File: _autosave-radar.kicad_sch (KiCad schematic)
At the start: 3 parts, among them J1 USB_C_Receptacle, J2 Conn_01x02_Pin, U1 BQ25895RTW

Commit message: expanding size of schematic
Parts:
- removed J2: Conn_01x02_Pin, symbol Connector:Conn_01x02_Pin
- added BT1: Battery_Cell, symbol Device:Battery_Cell
- added C1: 0.047muF, symbol Device:C
- added L1: 2.2muH, symbol Device:L
- added R1: 30K, symbol Device:R_US
- added R1: 5K, symbol Device:R_US
- added R3: 20muF, symbol Device:R_US
- added TH1: 103AT, symbol Device:Thermistor_NTC_US
- added U2: TPS61022, Package_DFN_QFN:Texas_RWU0007A_VQFN-7_2x2mm_P0.5mm, symbol Converter_DCDC:TPS61022
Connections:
- net GND: now reaches J1.A1 (GND), J1.A12 (GND), J1.B1 (GND), J1.B12 (GND)
- net GND: now also U1.17 (PGND), U1.18 (PGND), U1.25 (PGND), U1.8 (OTG), R1.1, TH1.1, U2.1 (GND)
- net at J1.A4 (VBUS), J1.A9 (VBUS), J1.B4 (VBUS)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: now also U1.1 (VBUS)
- net at U1.11 (TS): now also R1.1, R1.2
- net at U1.13 (BAT), U1.14 (BAT): now also BT1.2 (-)
- net at U1.15 (SYS), U1.16 (SYS): now also C1.1, R3.2
- net at U1.19 (SW), U1.20 (SW): now also L1.2
- net at U1.2 (D+): now also U1.3 (D-)
- net at U1.21 (BTST): now also C1.2
- net at U1.22 (REGN): now also R1.2, TH1.2
- new net: L1.1, R3.1
- no-connect marks 0 -> 2
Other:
- moved on the sheet: U1

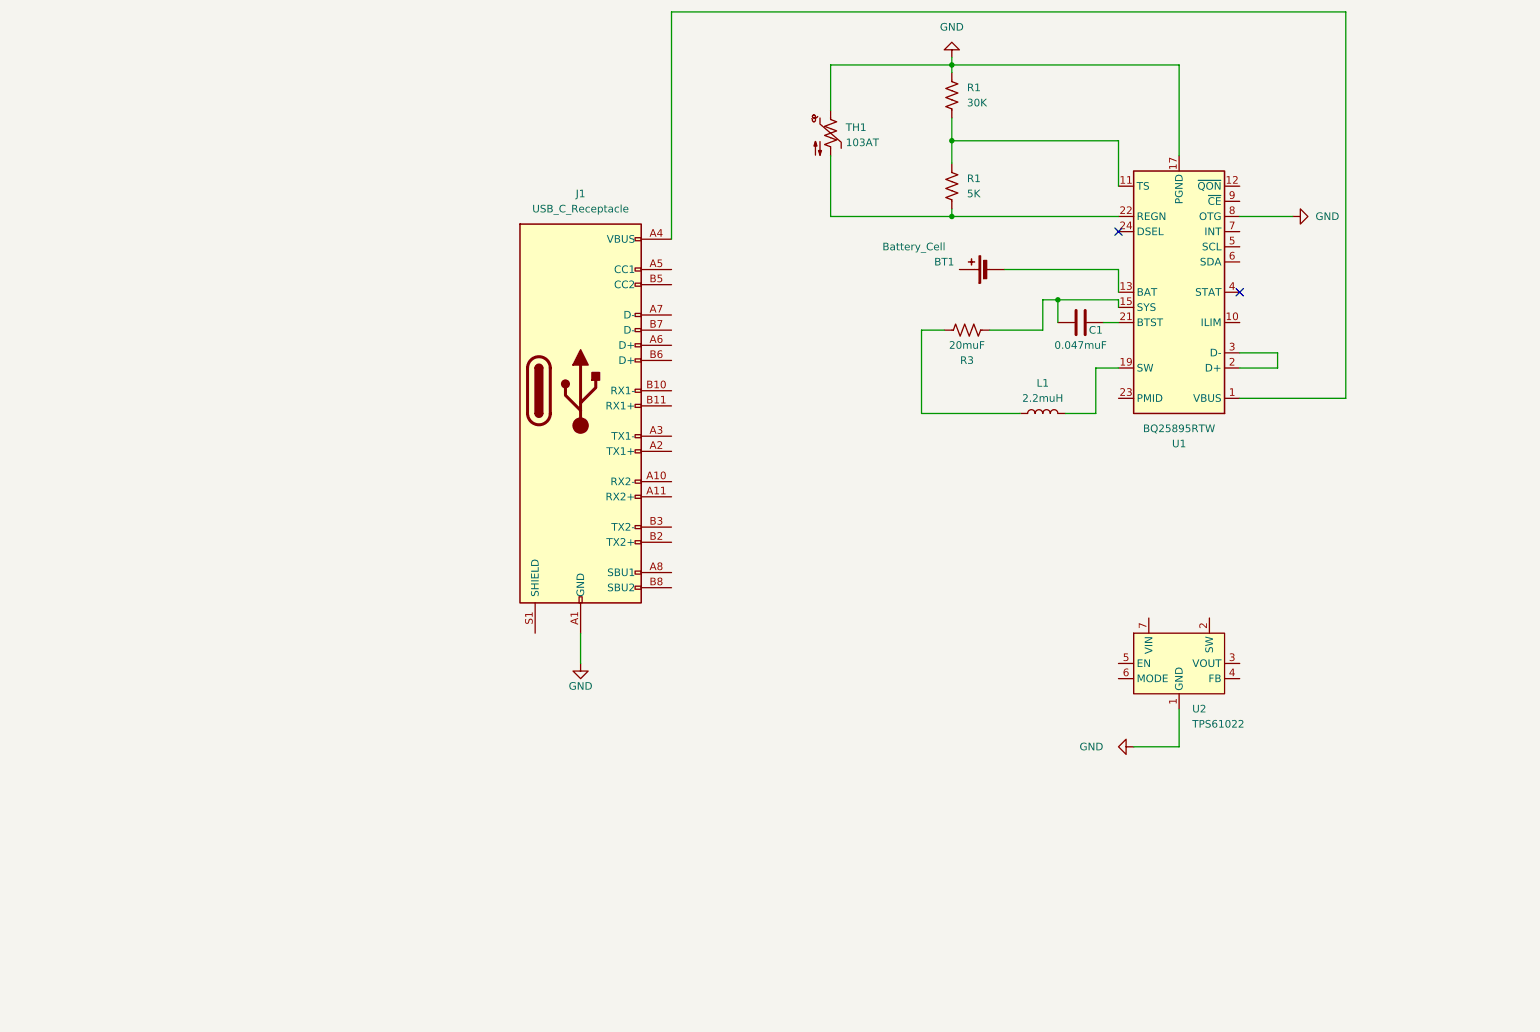
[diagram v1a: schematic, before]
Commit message: adding another sheet, stm32h7 core
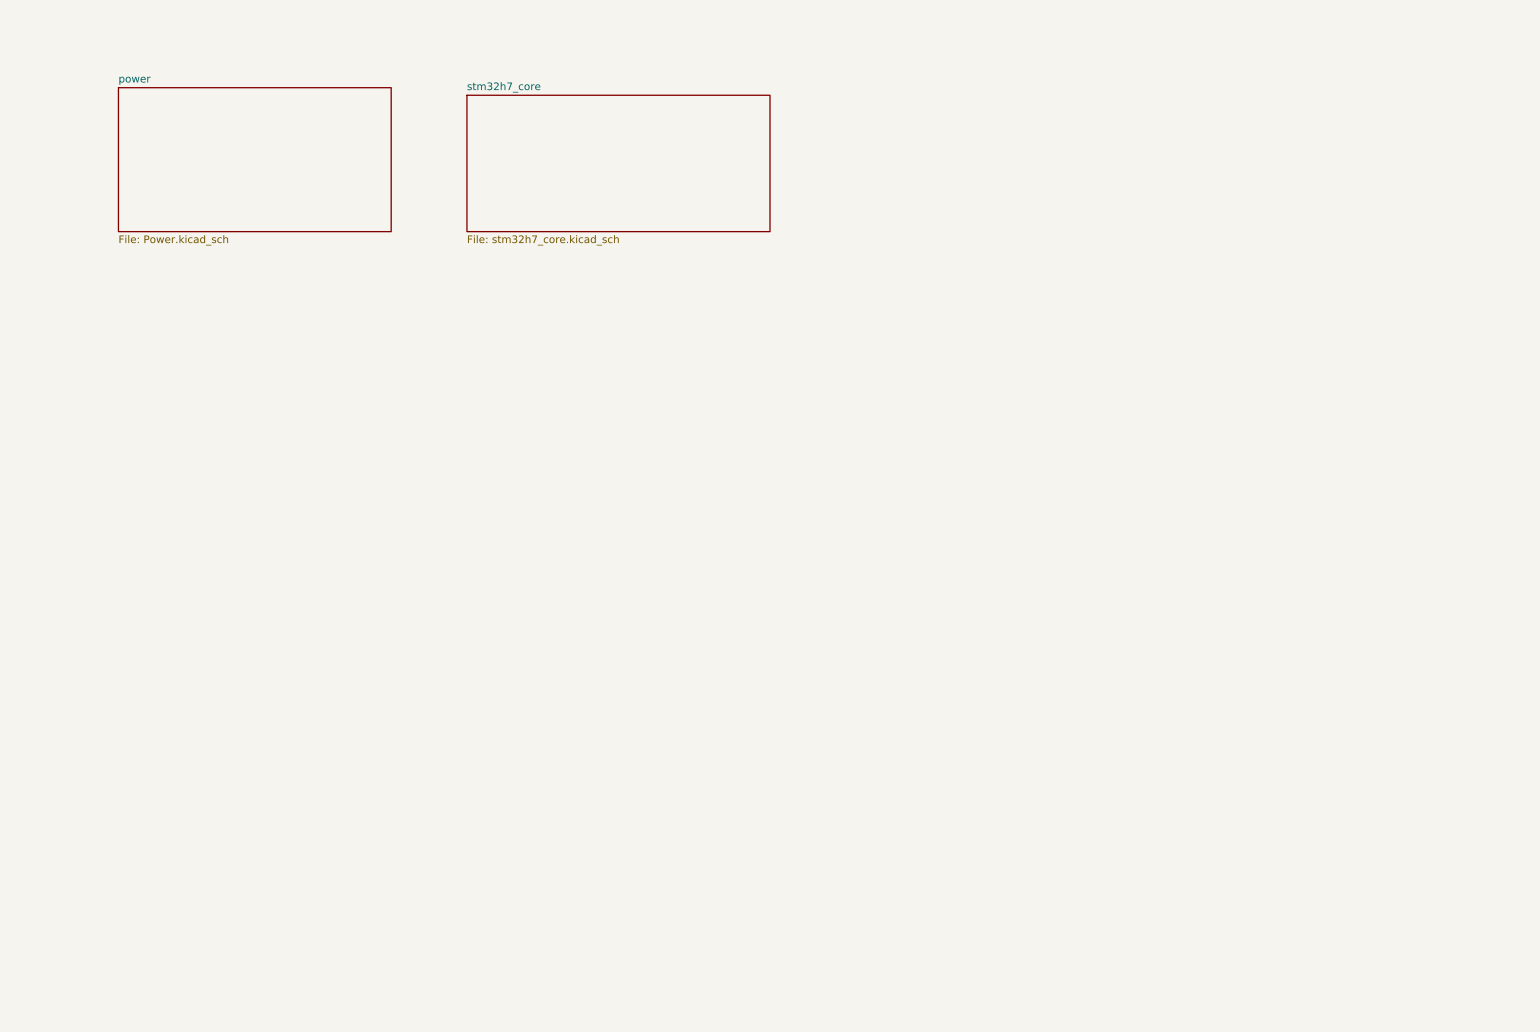
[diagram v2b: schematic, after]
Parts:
- removed BT1: Battery_Cell, symbol Device:Battery_Cell
- removed C1: 0.047muF, symbol Device:C
- removed J1: USB_C_Receptacle, symbol Connector:USB_C_Receptacle
- removed L1: 2.2muH, symbol Device:L
- removed R1: 30K, symbol Device:R_US
- removed R1: 5K, symbol Device:R_US
- removed R3: 20muF, symbol Device:R_US
- removed TH1: 103AT, symbol Device:Thermistor_NTC_US
- removed U1: BQ25895RTW, Package_DFN_QFN:Texas_RTW_WQFN-24-1EP_4x4mm_P0.5mm_EP2.7x2.7mm_ThermalVias, symbol Battery_Management:BQ25895RTW
- removed U2: TPS61022, Package_DFN_QFN:Texas_RWU0007A_VQFN-7_2x2mm_P0.5mm, symbol Converter_DCDC:TPS61022
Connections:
- no-connect marks 2 -> 0
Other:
- added sheet power (Power.kicad_sch)
- added sheet stm32h7_core (stm32h7_core.kicad_sch)

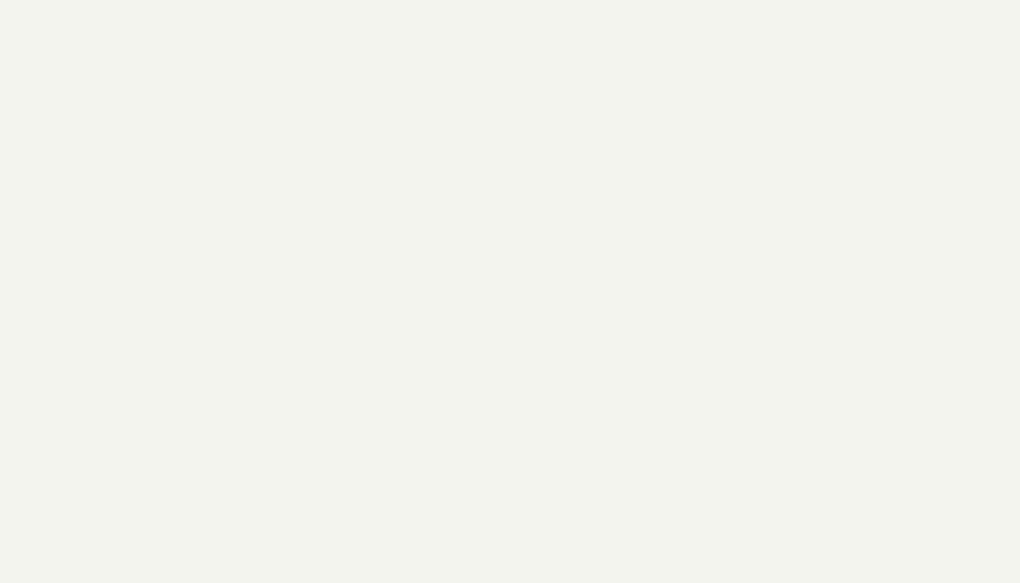
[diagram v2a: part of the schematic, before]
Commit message: rm stm32h7 going with awr1843 for our needs
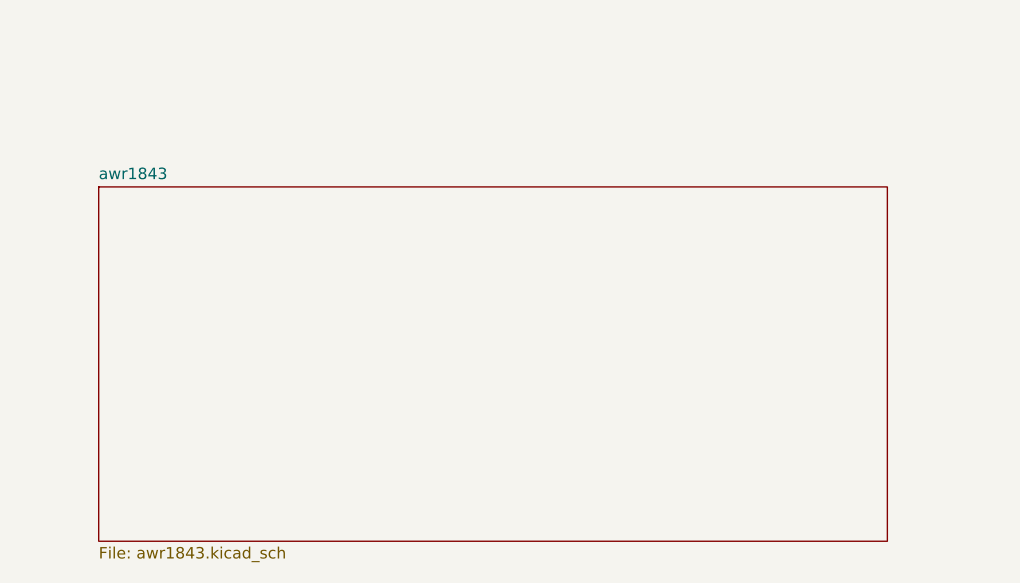
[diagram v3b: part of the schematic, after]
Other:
- added sheet awr1843 (awr1843.kicad_sch)
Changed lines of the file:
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@@
+    )
+  )
+  (sheet (at 43.18 81.28) (size 87.63 39.37) (fields_autoplaced)
+    (stroke (width 0.1524) (type solid))
+    (fill (color 0 0 0 0.0000))
+    (property "Sheetname" "awr1843" (at 43.18 80.5684 0)
+      (effects (font (size 1.27 1.27)) (justify left bottom))
+    )
+    (property "Sheetfile" "awr1843.kicad_sch" (at 43.18 121.2346 0)
+      (effects (font (size 1.27 1.27)) (justify left top))
+    )
+    (instances
+      (project "radar"
+        (path "/88b309aa-5f0e-45d7-beec-81d4b0ee2121" (page "4"))
+      )
     )
   )

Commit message: working on connectors
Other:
- removed sheet stm32h7_core
- added sheet connectors (cntors.kicad_sch)
- note added: "All PMICs of the board"
- note added: "The brain, functions as the MCU & RF signal TX/RX"
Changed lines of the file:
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@@
 (kicad_sch (version 20230121) (generator eeschema)
   (paper "A4")
-  (sheet (at 92.71 30.48) (size 50.8 22.86) (fields_autoplaced)
+  (text "The brain, functions as the MCU & RF signal TX/RX" (at 21.59 78.74 0)
+    (effects (font (size 2 2)) (justify left bottom))
+  )
+  (text "All PMICs of the board" (at 36.83 140.97 0)
+    (effects (font (size 2 2)) (justify left bottom))
+  )
+  (sheet (at 24.13 143.51) (size 62.23 39.37) (fields_autoplaced)
     (stroke (width 0.1524) (type solid))
     (fill (color 0 0 0 0.0000))
-    (property "Sheetname" "stm32h7_core" (at 92.71 29.7684 0)
+    (property "Sheetname" "power" (at 24.13 142.7984 0)
       (effects (font (size 1.27 1.27)) (justify left bottom))
     )
-    (property "Sheetfile" "stm32h7_core.kicad_sch" (at 92.71 53.9246 0)
+    (property "Sheetfile" "Power.kicad_sch" (at 24.13 183.4646 0)
       (effects (font (size 1.27 1.27)) (justify left top))
     )
-    (instances
-      (project "radar"
-        (path "/88b309aa-5f0e-45d7-beec-81d4b0ee2121" (page "3"))
-      )
-    )
-  )
-  (sheet (at 34.29 29.21) (size 45.72 24.13) (fields_autoplaced)
-    (stroke (width 0.1524) (type solid))
-    (fill (color 0 0 0 0.0000))
-    (property "Sheetname" "power" (at 34.29 28.4984 0)
-      (effects (font (size 1.27 1.27)) (justify left bottom))
-    )
-    (property "Sheetfile" "Power.kicad_sch" (at 34.29 53.9246 0)
-      (effects (font (size 1.27 1.27)) (justify left top))
-    )
-    (property "Field2" "" (at 34.29 29.21 0)
+    (property "Field2" "" (at 24.13 143.51 0)
       (effects (font (size 1.27 1.27)) hide)
     )
@@
     )
   )
-  (sheet (at 43.18 81.28) (size 87.63 39.37) (fields_autoplaced)
+  (sheet (at 16.51 82.55) (size 87.63 39.37) (fields_autoplaced)
     (stroke (width 0.1524) (type solid))
     (fill (color 0 0 0 0.0000))
-    (property "Sheetname" "awr1843" (at 43.18 80.5684 0)
+    (property "Sheetname" "awr1843" (at 16.51 81.8384 0)
       (effects (font (size 1.27 1.27)) (justify left bottom))
     )
-    (property "Sheetfile" "awr1843.kicad_sch" (at 43.18 121.2346 0)
+    (property "Sheetfile" "awr1843.kicad_sch" (at 16.51 122.5046 0)
       (effects (font (size 1.27 1.27)) (justify left top))
     )
@@
       )
     )
+  )
+  (sheet (at 160.02 111.76) (size 110.49 45.72) (fields_autoplaced)
+    (stroke (width 0.1524) (type solid))
+    (fill (color 0 0 0 0.0000))
+    (property "Sheetname" "connectors" (at 160.02 111.0484 0)
+      (effects (font (size 1.27 1.27)) (justify left bottom))
+    )
+    (property "Sheetfile" "cntors.kicad_sch" (at 160.02 158.0646 0)
+      (effects (font (size 1.27 1.27)) (justify left top))
+    )
+    (instances
+      (project "radar"
+        (path "/88b309aa-5f0e-45d7-beec-81d4b0ee2121" (page "5"))
+      )
+    )
